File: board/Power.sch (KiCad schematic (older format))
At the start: 46 parts

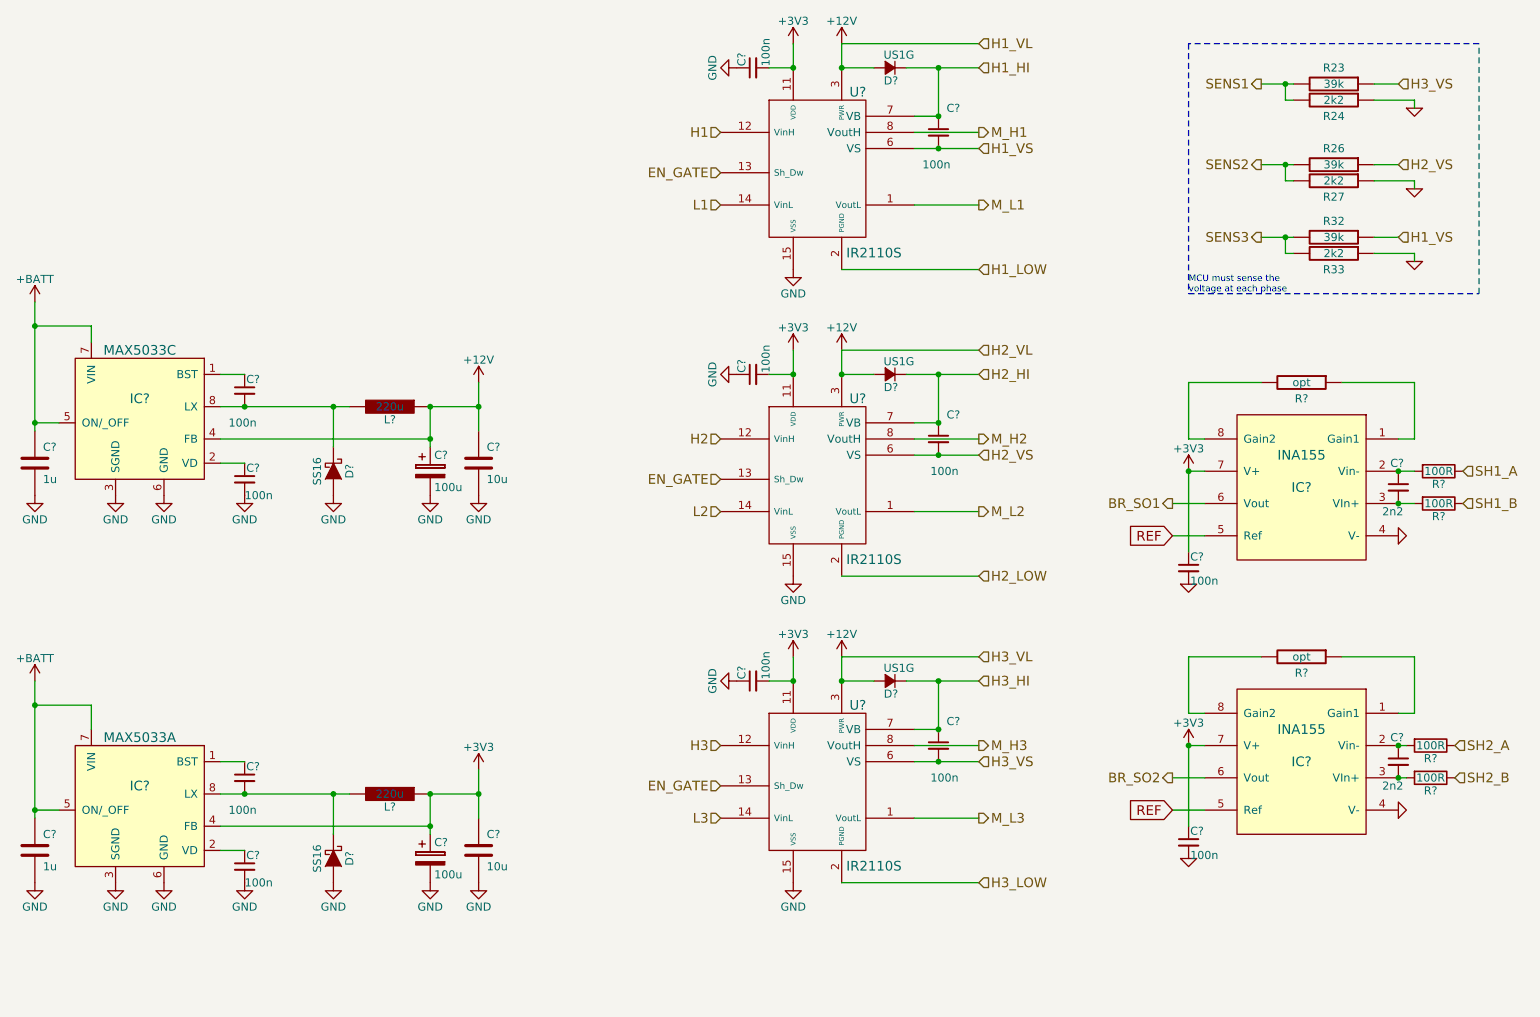
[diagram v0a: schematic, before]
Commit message: - implemented complementary transistor package - started layout
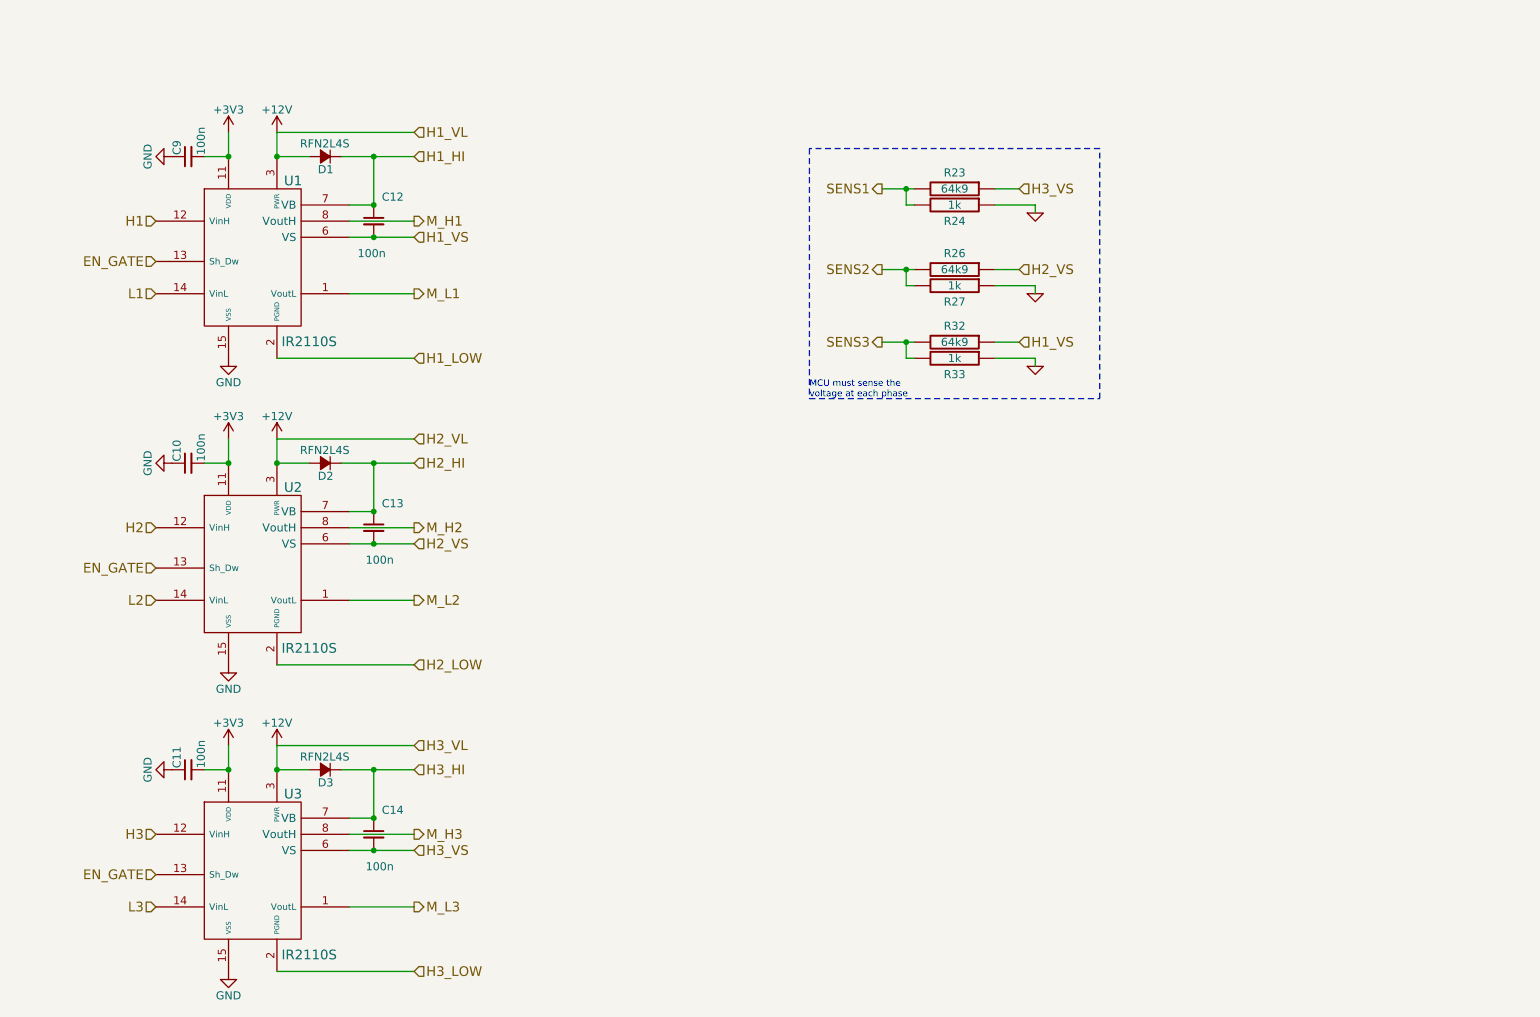
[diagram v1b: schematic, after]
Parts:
- removed C? (x6): 100n, symbol C_Small
- removed C? (x2): 2n2, symbol C_Small
- removed C? (x2): 10u, CRF1:SMD-0603_c, symbol C-RESCUE-BLDC_4
- removed C? (x2): 100u, symbol CP
- removed C? (x2): 1u, CRF1:SMD-0603_c, symbol C-RESCUE-BLDC_4
- removed D? (x2): SS16, symbol D_Schottky
- removed IC? (x2): INA155, symbol INA155
- removed IC?: MAX5033C, symbol MAX5033
- removed IC?: MAX5033A, symbol MAX5033
- removed L? (x2): 220u, symbol L
- removed R? (x2): opt, CRF1:SMD-0603_r, symbol R-RESCUE-BLDC_4
- removed R? (x4): 100R, symbol R
- C10, C11, C12, C13, C14, C9: renamed from C?; footprint (none) -> Capacitors_SMD:C_0805
- D1, D2, D3: renamed from D?; value US1G -> RFN2L4S; footprint (none) -> Diodes_SMD:SMA_Standard
- R23, R26, R32: value 39k -> 64k9; footprint CRF1:SMD-0603_r -> Resistors_SMD:R_0805
- R24, R27, R33: value 2k2 -> 1k; footprint CRF1:SMD-0603_r -> Resistors_SMD:R_0805
- U1, U2, U3: renamed from U?; footprint (none) -> Housings_SOIC:SOIC-16_7.5x10.3mm_Pitch1.27mm
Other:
- moved on the sheet: C10, C11, C12, C13, C14, C9, D1, D2, D3, R23, R24, R26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
